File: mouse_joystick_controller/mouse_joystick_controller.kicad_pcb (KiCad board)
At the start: 4 copper layers, 42 x 42 mm, 9 parts, among them J1 DA15_Plug

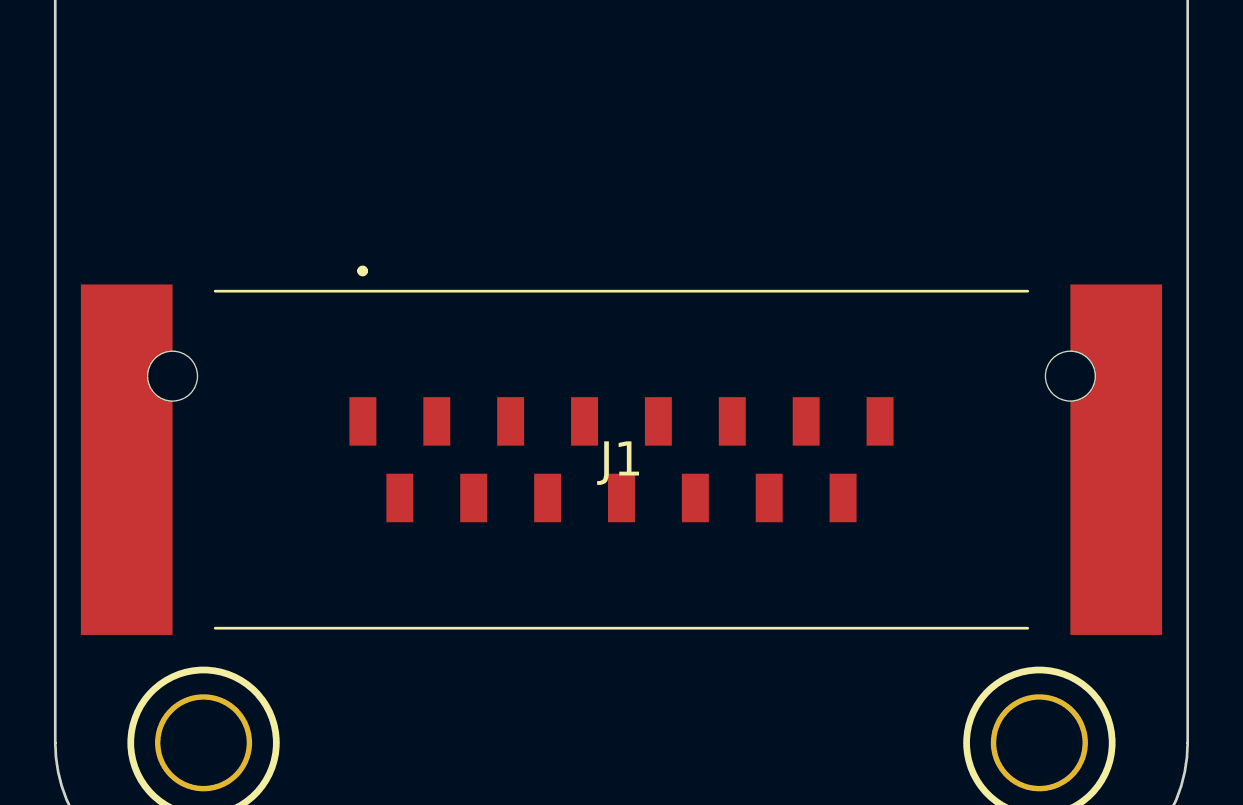
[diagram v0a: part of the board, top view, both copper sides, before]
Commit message: Add some driver components
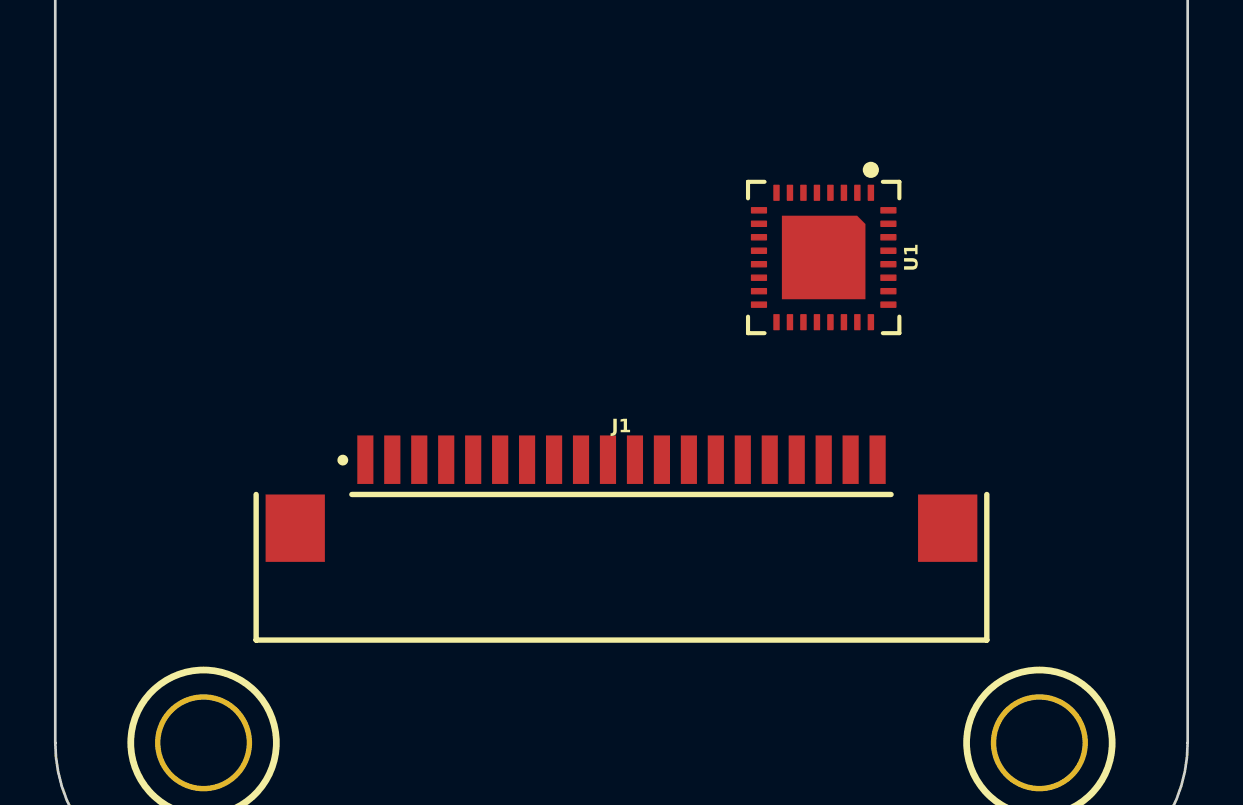
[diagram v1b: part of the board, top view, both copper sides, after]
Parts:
- added U1: LVDS_4-4_HALF_DS91M040TSQE, Janelia:DS91M040TSQE_NOPB, F.Cu at (157.5, 97.5)
- J1: value DA15_Plug -> Conn_FFC_20_Pin_1mm_bottom-ZF1-20-01-T-WT-TR; footprint Janelia:DSUB-15_Male_Vertical_SMD_09552296812741 -> Janelia:FFC_Samtec_ZF1-20-01-X-WT-Xx20-1MP_P1mm_Horizontal
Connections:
- J1 pad 16: (no net) -> unconnected-(J1-Pin_16-Pad16)
- J1 pad 17: (no net) -> unconnected-(J1-Pin_17-Pad17)

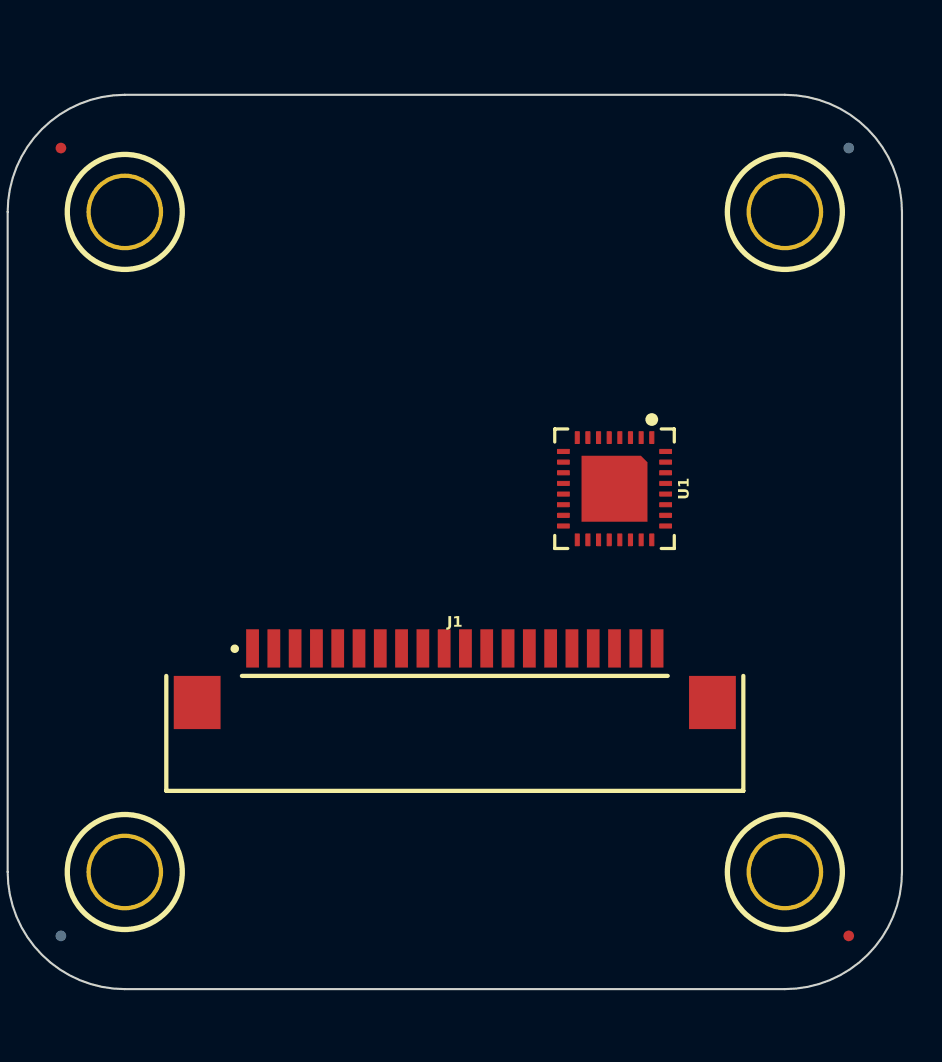
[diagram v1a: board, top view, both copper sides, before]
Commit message: Rearrange sheets
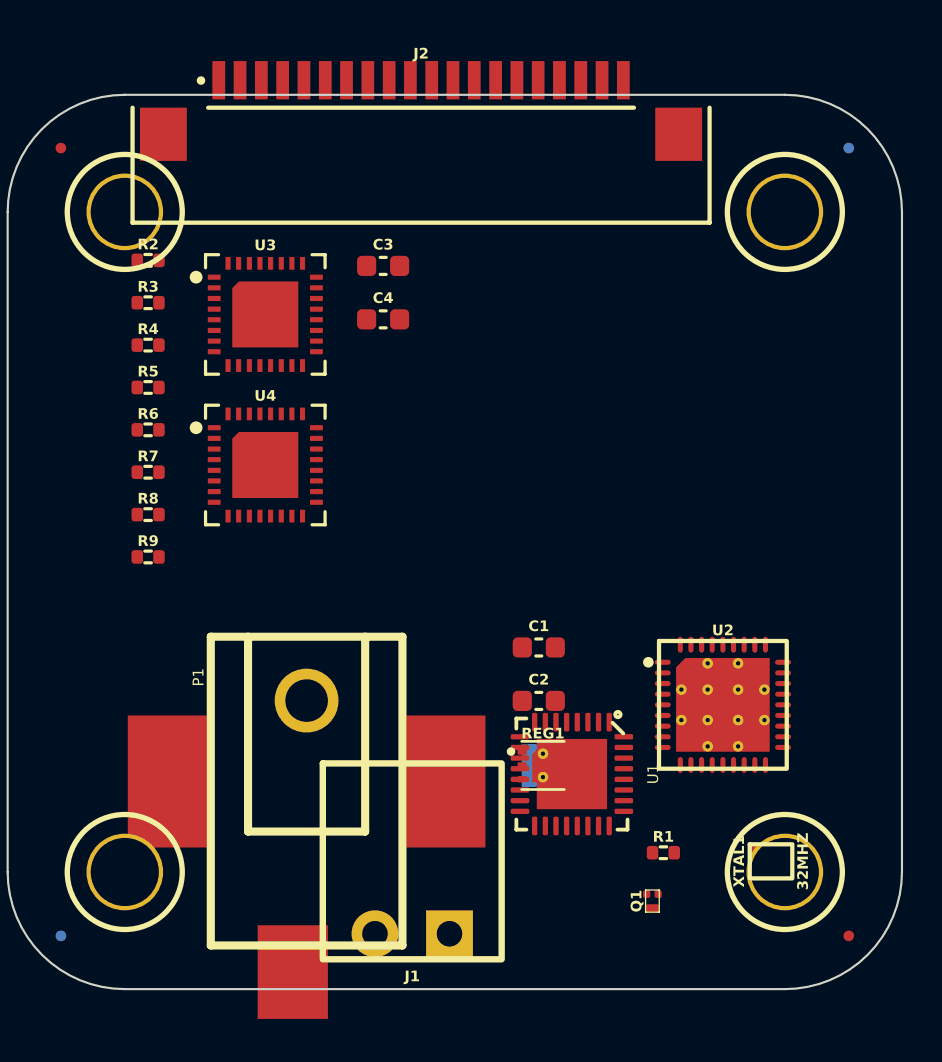
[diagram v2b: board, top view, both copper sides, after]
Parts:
- added C1: 1uF_50V, Janelia:C_0603_1608Metric, F.Cu at (153.9, 105.0)
- added C2: 2.2uF_50V, Janelia:C_0603_1608Metric, F.Cu at (153.9, 107.5)
- added C3: 0.1uF_50V, Janelia:C_0603_1608Metric, F.Cu at (146.6, 87.0)
- added C4: 0.1uF_50V, Janelia:C_0603_1608Metric, F.Cu at (146.6, 89.5)
- added J2: Conn_FFC_20_Pin_1mm_bottom-ZF1-20-01-T-WT-TR, Janelia:FFC_Samtec_ZF1-20-01-X-WT-Xx20-1MP_P1mm_Horizontal, F.Cu at (148.4, 78.3)
- added P1: PWR_JACK_2.1x5.5_SMD_RA, Janelia:DCJACK_3PAD_SMD_RA, F.Cu at (143.0, 104.5)
- added Q1: MOSFET-N-CH, Janelia:XFDFN-3, F.Cu at (159.3, 116.9)
- added R1: 1k, Janelia:R_0402_1005Metric, F.Cu at (159.8, 114.6)
- added R2: 100, Janelia:R_0402_1005Metric, F.Cu at (135.6, 86.8)
- added R3: 100, Janelia:R_0402_1005Metric, F.Cu at (135.6, 88.8)
- added R4: 100, Janelia:R_0402_1005Metric, F.Cu at (135.6, 90.8)
- added R5: 100, Janelia:R_0402_1005Metric, F.Cu at (135.6, 92.7)
- added R6: 100, Janelia:R_0402_1005Metric, F.Cu at (135.6, 94.7)
- added R7: 100, Janelia:R_0402_1005Metric, F.Cu at (135.6, 96.7)
- added R8: 100, Janelia:R_0402_1005Metric, F.Cu at (135.6, 98.7)
- added R9: 100, Janelia:R_0402_1005Metric, F.Cu at (135.6, 100.7)
- added REG1: 3.3V_150MA, Janelia:SON65P200X200X80-7N, F.Cu at (154.1, 110.5)
- added U2: PGA305ARHHR, Janelia:RHH0036C, F.Cu at (162.6, 107.7)
- added U3: LVDS_4-4_HALF_DS91M040TSQE, Janelia:DS91M040TSQE_NOPB, F.Cu at (141.1, 89.3)
- added U4: LVDS_4-4_HALF_DS91M040TSQE, Janelia:DS91M040TSQE_NOPB, F.Cu at (141.1, 96.4)
- added XTAL1: 32MHZ, Janelia:XTAL_WURTH_IQX0-540, F.Cu at (164.8, 115.0)
- J1: value Conn_FFC_20_Pin_1mm_bottom-ZF1-20-01-T-WT-TR -> Conn_TERM_HDR_01x02_Pin_3.5MM_Horizontal; footprint Janelia:FFC_Samtec_ZF1-20-01-X-WT-Xx20-1MP_P1mm_Horizontal -> Janelia:TERM_HDR_01x02_Pin_Horizontal_3.5MM_1844210
- U1: value LVDS_4-4_HALF_DS91M040TSQE -> TMC429; footprint Janelia:DS91M040TSQE_NOPB -> Janelia:QFN-32-1EP_5x5mm_P0.5mm_EP3.3x3.3mm
- moved J1 13.5 mm to (148.0, 118.4)
- moved U1 13.5 mm to (155.5, 110.9)
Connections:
- net /assembly/GND renamed /GND
- J1 pad 1: unconnected-(J1-Pin_1-Pad1) -> /brake/+24V
- J1 pad 2: unconnected-(J1-Pin_2-Pad2) -> /brake/BRAKE-
- U1 pad 11: unconnected-(U1-VDD-Pad11) -> (no net)
- U1 pad 16: unconnected-(U1-DE3-Pad16) -> (no net)
- U1 pad 23: /driver_0/STEP_A -> unconnected-(U1-GND-Pad23)
- U1 pad 24: /driver_0/STEP_B -> (no net)
- U1 pad 26: unconnected-(U1-~{RE0}-Pad26) -> (no net)
- U1 pad 32: unconnected-(U1-FSEN1-Pad32) -> (no net)
- U1 pad 9: unconnected-(U1-FSEN2-Pad9) -> (no net)

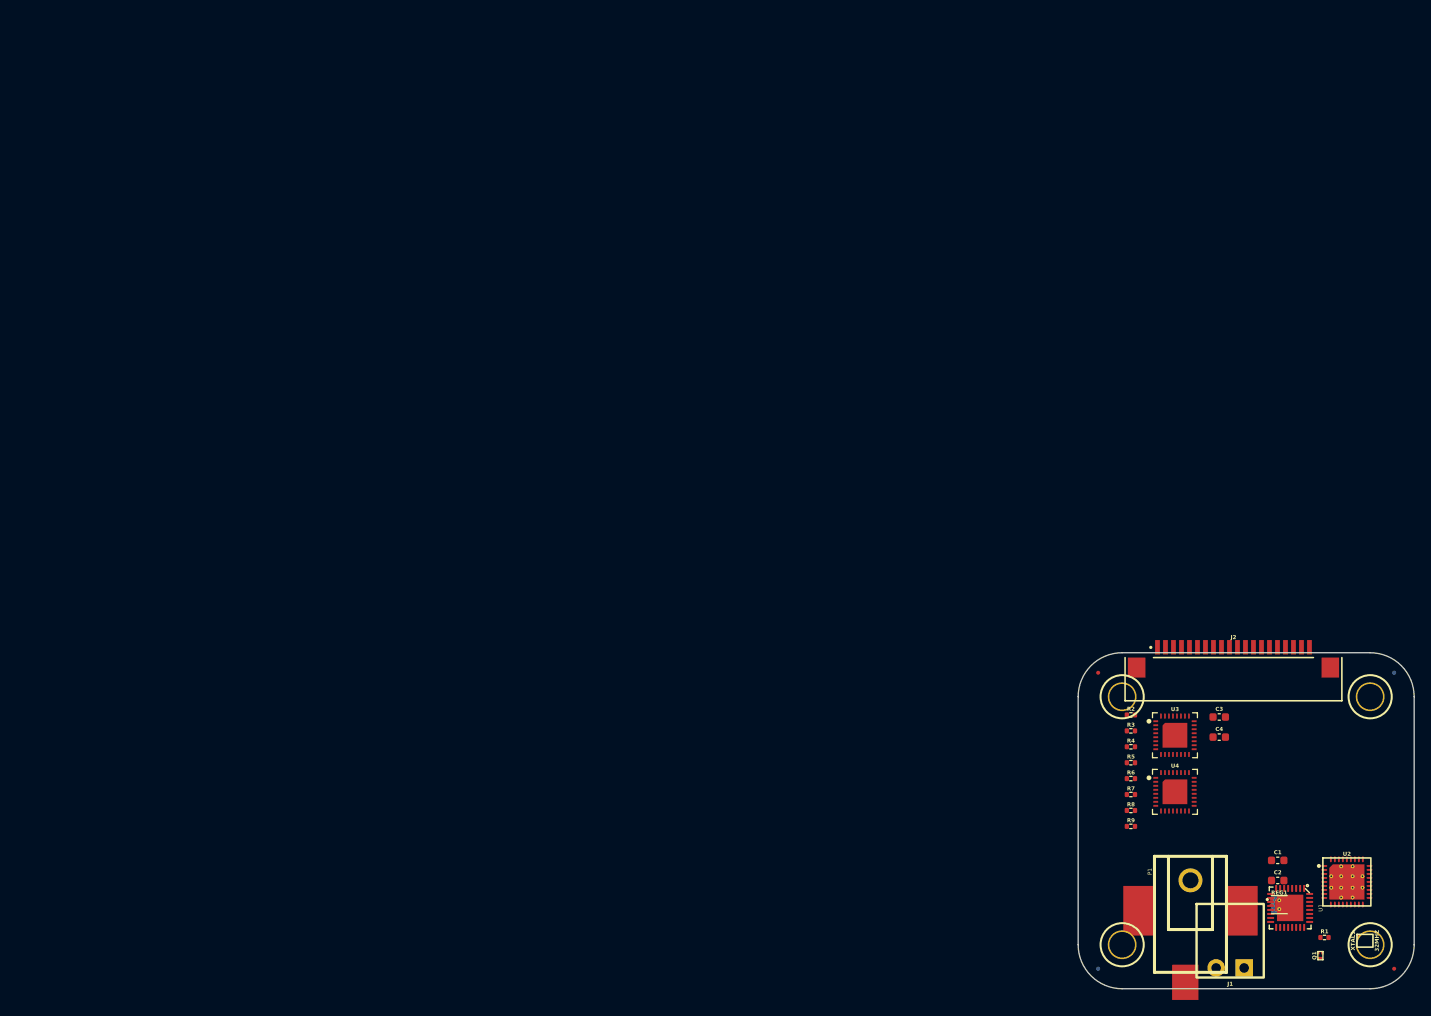
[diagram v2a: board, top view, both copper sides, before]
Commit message: Test pin rcpt
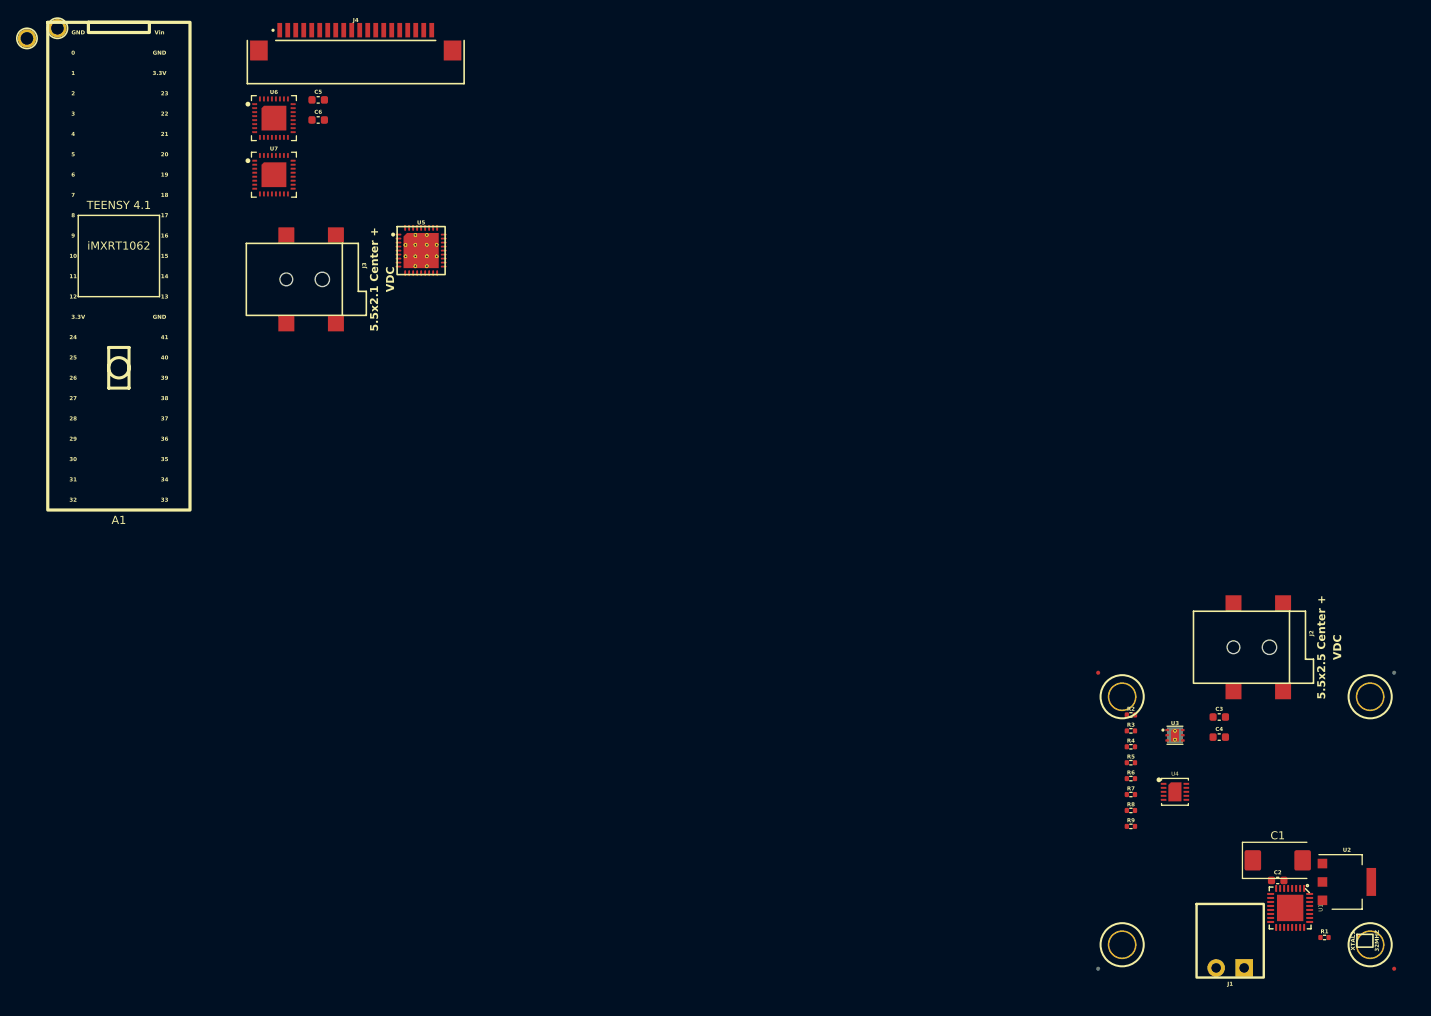
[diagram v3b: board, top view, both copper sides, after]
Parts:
- removed P1: PWR_JACK_2.1x5.5_SMD_RA, Janelia:DCJACK_3PAD_SMD_RA
- removed Q1: MOSFET-N-CH, Janelia:XFDFN-3
- removed REG1: 3.3V_150MA, Janelia:SON65P200X200X80-7N
- added A1: TEENSY_4.1_PIN_RECEPTACLES, Janelia:TEENSY_4.1_PIN_RECEPTACLES, F.Cu at (9.09, 18.0)
- added C5: 0.1uF_50V, Janelia:C_0603_1608Metric, F.Cu at (34.0, 9.89)
- added C6: 0.1uF_50V, Janelia:C_0603_1608Metric, F.Cu at (34.0, 12.4)
- added J3: 5.5x2.1_SMD_RA, Janelia:CONN_54-00164, F.Cu at (30.0, 32.3)
- added J4: Conn_FFC_20_Pin_1mm_bottom-ZF1-20-01-T-WT-TR, Janelia:FFC_Samtec_ZF1-20-01-X-WT-Xx20-1MP_P1mm_Horizontal, F.Cu at (38.7, 1.18)
- added PR0: Conn_Pin_Rcpt-0305-1-15, Janelia:CONN_PIN_RCPT-0305-1-15, F.Cu at (1.41, 0.94)
- added PR1: Conn_Pin_Rcpt-0305-1-15, Janelia:CONN_PIN_RCPT-0305-1-15, F.Cu at (-2.40, 2.21)
- added U5: PGA305ARHHR, Janelia:RHH0036C, F.Cu at (46.9, 28.7)
- added U6: LVDS_4-4_HALF_DS91M040TSQE, Janelia:DS91M040TSQE_NOPB, F.Cu at (28.5, 12.2)
- added U7: LVDS_4-4_HALF_DS91M040TSQE, Janelia:DS91M040TSQE_NOPB, F.Cu at (28.5, 19.2)
- C1: value 1uF_50V -> 47uF_35V; footprint Janelia:C_0603_1608Metric -> Janelia:CP_EIA-7343-43_Kemet-X
- C2: value 2.2uF_50V -> 10uF_35V
- C3: value 0.1uF_50V -> 1uF_50V
- C4: value 0.1uF_50V -> 2.2uF_50V
- J2: value Conn_FFC_20_Pin_1mm_bottom-ZF1-20-01-T-WT-TR -> 5.5x2.5_SMD_RA; footprint Janelia:FFC_Samtec_ZF1-20-01-X-WT-Xx20-1MP_P1mm_Horizontal -> Janelia:CONN_54-00165
- R1: value 1k -> 22
- U2: value PGA305ARHHR -> NCR421ZX; footprint Janelia:RHH0036C -> Janelia:SOT-223
- U3: value LVDS_4-4_HALF_DS91M040TSQE -> 3.3V_150MA; footprint Janelia:DS91M040TSQE_NOPB -> Janelia:SON65P200X200X80-7N
- U4: value LVDS_4-4_HALF_DS91M040TSQE -> AD9837ACPZ-RL; footprint Janelia:DS91M040TSQE_NOPB -> Janelia:DFN-10_DD_LIT-L
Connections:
- C1 pad 1: /+24V -> /brake/BRAKE+
- C1 pad 2: /GND -> /brake/GND
- C2 pad 1: /power/3.3V -> /brake/BRAKE+
- C2 pad 2: /GND -> /brake/GND
- C3 pad 1: /motors/+3.3V -> /+24V
- C3 pad 2: /motors/GND -> /GND
- C4 pad 1: /motors/+3.3V -> /power/3.3V
- C4 pad 2: /motors/GND -> /GND
- J1 pad 1: /brake/+24V -> /brake/BRAKE+
- J2 pad 1: /motors/GND -> /+24V
- J2 pad 2: /motors/GND -> /GND
- J2 pad 3: /motors/driver_0/VAA -> unconnected-(J2-Pad3)
- R1 pad 1: /brake/BRAKE_PWM -> /brake/R_EXT
- R9 pad 1: /motors/driver_0/POWER_ENABLE_A -> /motors/driver_0/STANDBY_A
- R9 pad 2: /motors/driver_0/POWER_ENABLE_B -> /motors/driver_0/STANDBY_B
- U2 pad 1: (no net) -> /brake/BRAKE_PWM
- U2 pad 2: unconnected-(U2-DVDD_MEM-Pad2) -> /brake/R_EXT
- U2 pad 3: unconnected-(U2-DVDD-Pad3) -> /brake/GND
- U2 pad 4: (no net) -> /brake/BRAKE-
- U3 pad 1: unconnected-(U3-RO0-Pad1) -> /+3.3V
- U3 pad 2: /motors/STEP_0 -> (no net)
- U3 pad 3: unconnected-(U3-RO1-Pad3) -> /GND
- U3 pad 4: /motors/DIR_0 -> unconnected-(U3-EN-Pad4)
- U3 pad 5: unconnected-(U3-RO2-Pad5) -> (no net)
- U3 pad 6: /motors/UART_TX_ENABLE_0 -> /+24V
- U3 pad 7: /motors/UART_RX_0 -> /GND
- U4 pad 10: /motors/+3.3V -> unconnected-(U4-VOUT-Pad10)
- U4 pad 11: /motors/+3.3V -> unconnected-(U4-PAD-Pad11)
- U4 pad 2: /motors/~{DRIVER_ENABLE_0} -> unconnected-(U4-VDD-Pad2)
- U4 pad 3: /motors/REF_0 -> unconnected-(U4-CAP-Pad3)
- U4 pad 4: /motors/GND -> unconnected-(U4-DGND-Pad4)
- U4 pad 5: /motors/REFR_0 -> unconnected-(U4-MCLK-Pad5)
- U4 pad 6: /motors/GND -> unconnected-(U4-SDATA-Pad6)
- U4 pad 8: /motors/POWER_ENABLE_0 -> unconnected-(U4-FSYNC-Pad8)
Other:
- board outline removed
